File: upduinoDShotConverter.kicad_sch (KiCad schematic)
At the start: 11 parts, among them J1 ESC_OUT, J2 5V and Buzzer In, J3 VBAT_and_motors_1-4_in, J5 Motors_5-8_in

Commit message: lots of tweaks, solid design. About to attempt orientation shift
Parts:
- added J4, J6: Conn_01x24_Pin, Connector_PinHeader_2.54mm:PinHeader_1x24_P2.54mm_Vertical, symbol Connector:Conn_01x24_Pin
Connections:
- net +3.3V: now also J4.9 (Pin_9)
- net +5V: now also J4.8 (Pin_8)
- net GND: now also J4.1 (Pin_1), J4.10 (Pin_10), J6.18 (Pin_18)
- net at J1.4 (Pin_4), R1.2: now also U1.40 (gpio_12), J6.16 (Pin_16); no longer U1.27 (gpio_47)
- net at J3.3 (Pin_3), U1.22 (gpio_42): now also J4.22 (Pin_22)
- net at J3.4 (Pin_4), U1.21 (gpio_36): now also J4.21 (Pin_21)
- net at J3.5 (Pin_5), U1.20 (gpio_43): now also J4.20 (Pin_20)
- net at J3.6 (Pin_6), U1.19 (gpio_34): now also J4.19 (Pin_19)
- net at U1.11 (gpio_23): now also J4.11 (Pin_11)
- net at U1.12 (gpio_25): now also J4.12 (Pin_12)
- net at J5.4 (Pin_4), U1.13 (gpio_26): now also J4.13 (Pin_13)
- net at J5.3 (Pin_3), U1.14 (gpio_27): now also J4.14 (Pin_14)
- net at J5.2 (Pin_2), U1.15 (gpio_32): now also J4.15 (Pin_15)
- net at U1.16 (gpio_35): now also J4.16 (Pin_16)
- net at J5.1 (Pin_1), U1.17 (gpio_31): now also J4.17 (Pin_17)
- net at U1.18 (gpio_37): now also J4.18 (Pin_18)
- net at U1.2 (VIO): now also J4.2 (Pin_2)
- net at U1.23 (gpio_38): now also J4.23 (Pin_23)
- net at U1.24 (gpio_28): now also J4.24 (Pin_24)
- net at U1.25 (gpio_2): now also J6.1 (Pin_1)
- net at J1.3 (Pin_3), R2.2: now also U1.39 (gpio_21), J6.15 (Pin_15); no longer U1.26 (gpio_46)
- net at U1.28 (gpio_45): now also J6.4 (Pin_4)
- net at U1.29 (gpio_48): now also J6.5 (Pin_5)
- net at U1.3 (RST): now also J4.3 (Pin_3)
- net at U1.30 (gpio_3): now also J6.6 (Pin_6)
- net at U1.31 (gpio_4): now also J6.7 (Pin_7)
- net at U1.32 (gpio_44): now also J6.8 (Pin_8)
- net at U1.33 (gpio_6): now also J6.9 (Pin_9)
- net at U1.34 (gpio_9): now also J6.10 (Pin_10)
- net at U1.35 (gpio_11): now also J6.11 (Pin_11)
- net at U1.36 (gpio_18): now also J6.12 (Pin_12)
- net at U1.37 (gpio_19): now also J6.13 (Pin_13)
- net at U1.38 (gpio_13): now also J6.14 (Pin_14)
- net at U1.4 (DONE): now also J4.4 (Pin_4)
- net at U1.41 (12Mhz): now also J6.17 (Pin_17)
- net at U1.43 (gpio_10): now also J6.19 (Pin_19)
- net at U1.44 (gpio_20): now also J6.20 (Pin_20)
- net at U1.45 (spi_miso): now also J6.21 (Pin_21)
- net at U1.46 (spi_mosi): now also J6.22 (Pin_22)
- net at U1.47 (spi_sck): now also J6.23 (Pin_23)
- net at U1.48 (spi_ssn): now also J6.24 (Pin_24)
- net at U1.5 (RGB2): now also J4.5 (Pin_5)
- net at U1.6 (RGB0): now also J4.6 (Pin_6)
- net at U1.7 (RGB1): now also J4.7 (Pin_7)
- new net: J6.2 (Pin_2), U1.26 (gpio_46)
- new net: J6.3 (Pin_3), U1.27 (gpio_47)
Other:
- moved on the sheet: R1, R2

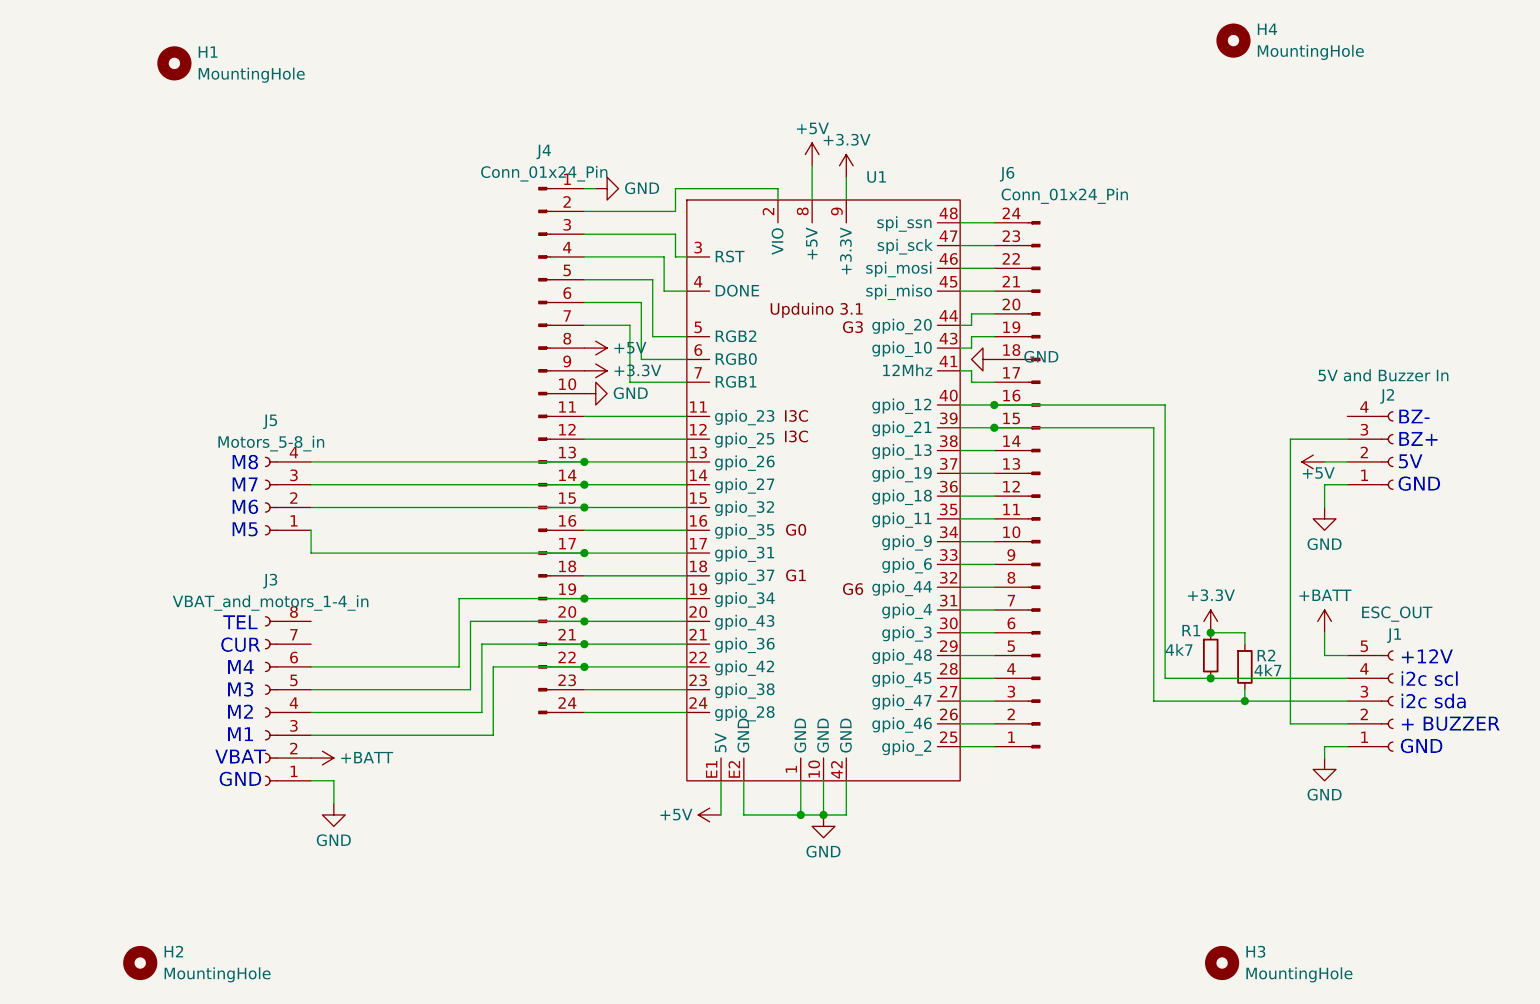
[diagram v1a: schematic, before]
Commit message: sucessful orientation shift, along with additional GPIO breakouts and via arrows
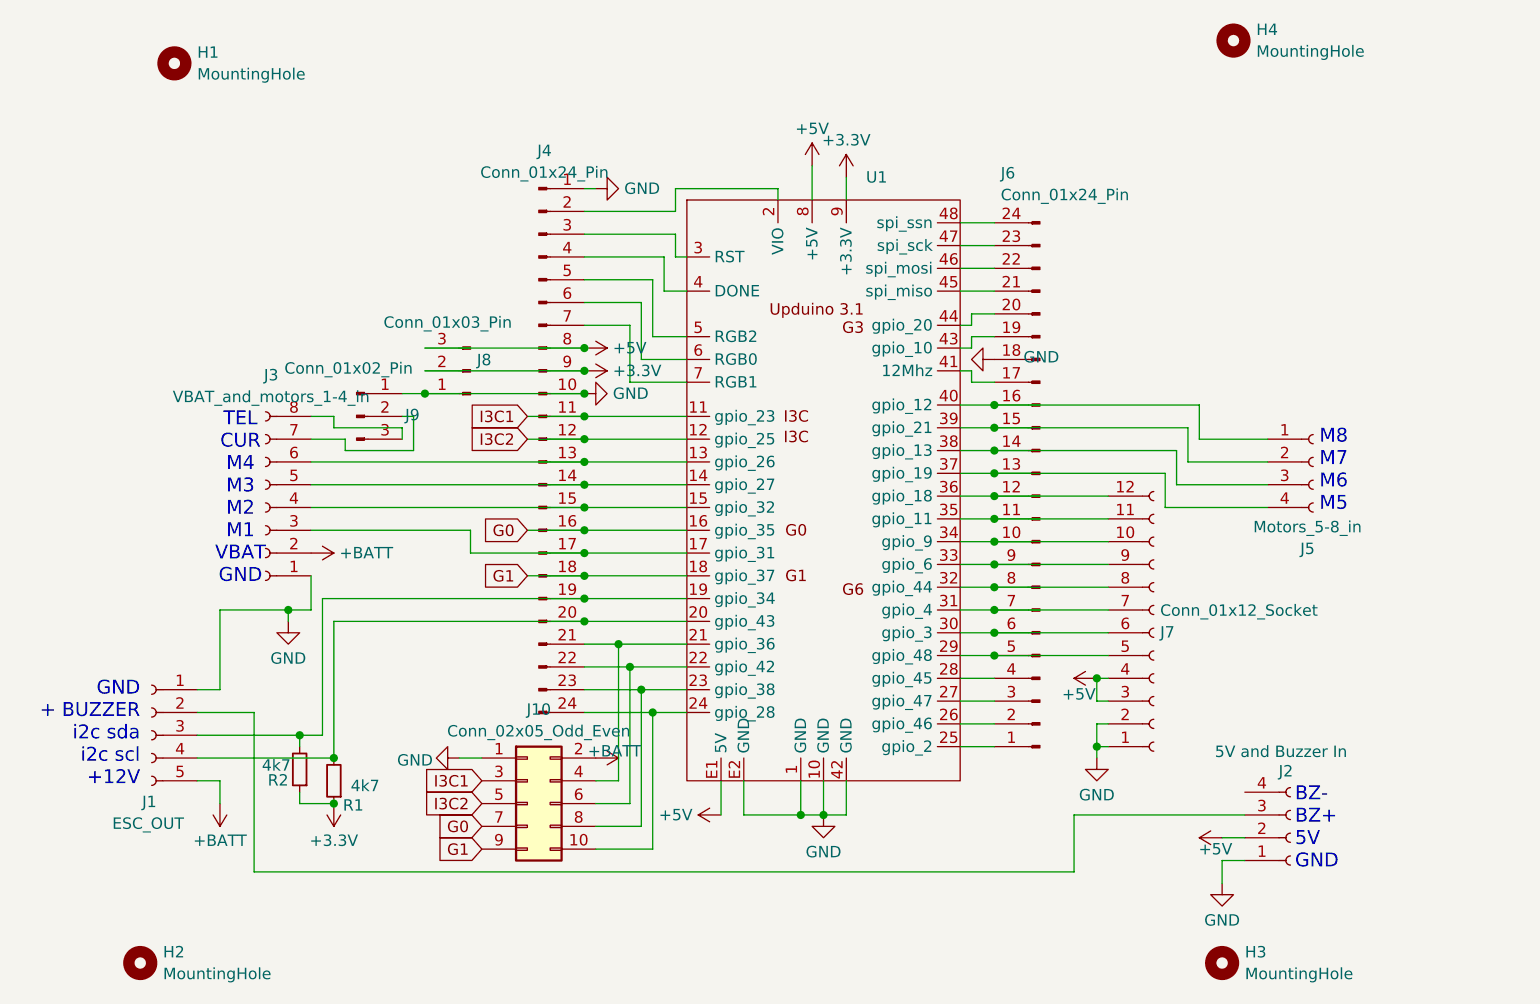
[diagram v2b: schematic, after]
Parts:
- added J10: Conn_02x05_Odd_Even, Connector_PinHeader_2.54mm:PinHeader_2x05_P2.54mm_Vertical, symbol Connector_Generic:Conn_02x05_Odd_Even
- added J7: Conn_01x12_Socket, Connector_JST:JST_SH_SM12B-SRSS-TB_1x12-1MP_P1.00mm_Horizontal, symbol Connector:Conn_01x12_Socket
- added J8: Conn_01x03_Pin, Connector_PinHeader_2.54mm:PinHeader_1x03_P2.54mm_Vertical, symbol Connector:Conn_01x03_Pin
- added J9: Conn_01x02_Pin, Connector_PinHeader_2.54mm:PinHeader_1x03_P2.54mm_Vertical, symbol Connector:Conn_01x03_Pin
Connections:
- net +3.3V: now also J8.2 (Pin_2)
- net +5V: now also J7.3 (Pin_3), J7.4 (Pin_4), J8.3 (Pin_3)
- net +BATT: now also J10.2 (Pin_2)
- net GND: now also J10.1 (Pin_1), J7.1 (Pin_1), J7.2 (Pin_2), J8.1 (Pin_1), J9.1 (Pin_1)
- net I3C1: now reaches J4.11 (Pin_11), U1.11 (gpio_23)
- net I3C1: now also J10.3 (Pin_3)
- net I3C2: now reaches J4.12 (Pin_12), U1.12 (gpio_25)
- net I3C2: now also J10.5 (Pin_5)
- net at J4.13 (Pin_13), U1.13 (gpio_26): now also J3.6 (Pin_6); no longer J5.4 (Pin_4)
- net at J4.14 (Pin_14), U1.14 (gpio_27): now also J3.5 (Pin_5); no longer J5.3 (Pin_3)
- net at J4.15 (Pin_15), U1.15 (gpio_32): now also J3.4 (Pin_4); no longer J5.2 (Pin_2)
- net G0: now reaches J4.16 (Pin_16), U1.16 (gpio_35)
- net G0: now also J10.7 (Pin_7)
- net at J4.17 (Pin_17), U1.17 (gpio_31): now also J3.3 (Pin_3); no longer J5.1 (Pin_1)
- net G1: now reaches J4.18 (Pin_18), U1.18 (gpio_37)
- net G1: now also J10.9 (Pin_9)
- net at J4.19 (Pin_19), U1.19 (gpio_34): now also J1.3 (Pin_3), R2.2; no longer J3.6 (Pin_6)
- net at J4.20 (Pin_20), U1.20 (gpio_43): now also J1.4 (Pin_4), R1.2; no longer J3.5 (Pin_5)
- net at J4.21 (Pin_21), U1.21 (gpio_36): now also J10.4 (Pin_4); no longer J3.4 (Pin_4)
- net at J4.22 (Pin_22), U1.22 (gpio_42): now also J10.6 (Pin_6); no longer J3.3 (Pin_3)
- net at J4.23 (Pin_23), U1.23 (gpio_38): now also J10.8 (Pin_8)
- net at J4.24 (Pin_24), U1.24 (gpio_28): now also J10.10 (Pin_10)
- net at J6.10 (Pin_10), U1.34 (gpio_9): now also J7.10 (Pin_10)
- net at J6.11 (Pin_11), U1.35 (gpio_11): now also J7.11 (Pin_11)
- net at J6.12 (Pin_12), U1.36 (gpio_18): now also J7.12 (Pin_12)
- net at J6.13 (Pin_13), U1.37 (gpio_19): now also J5.4 (Pin_4)
- net at J6.14 (Pin_14), U1.38 (gpio_13): now also J5.3 (Pin_3)
- net at J6.15 (Pin_15), U1.39 (gpio_21): now also J5.2 (Pin_2); no longer J1.3 (Pin_3), R2.2
- net at J6.16 (Pin_16), U1.40 (gpio_12): now also J5.1 (Pin_1); no longer J1.4 (Pin_4), R1.2
- net at J6.5 (Pin_5), U1.29 (gpio_48): now also J7.5 (Pin_5)
- net at J6.6 (Pin_6), U1.30 (gpio_3): now also J7.6 (Pin_6)
- net at J6.7 (Pin_7), U1.31 (gpio_4): now also J7.7 (Pin_7)
- net at J6.8 (Pin_8), U1.32 (gpio_44): now also J7.8 (Pin_8)
- net at J6.9 (Pin_9), U1.33 (gpio_6): now also J7.9 (Pin_9)
- net at J3.7 (Pin_7): now also J9.2 (Pin_2)
- net at J3.8 (Pin_8): now also J9.3 (Pin_3)
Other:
- note added: "GND + BUZZER i2c sda i2c scl +12V"
- note removed: "+12V i2c scl i2c sda + BUZZER GND"
- moved on the sheet: J1, J2, J3, J5, R1, R2
